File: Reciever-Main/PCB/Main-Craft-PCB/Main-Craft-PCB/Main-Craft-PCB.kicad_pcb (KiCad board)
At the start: 2 copper layers, 68.6 x 99.1 mm, 122 parts, among them J1 nRF24L01_Conn, J10 L298N, J2 IR_SENSOR_1, J3 IR_SENSOR_2, J4 IR_SENSOR_?, J5 IR_SENSOR_?, J6 ESC_1, J7 ESC_2, J8 ESC_3, J9 ESC_4, Q1 2N2219, Q10 2N2219, Q11 2N2219, Q12 2N2219, Q13 2N2219, Q14 2N2219, Q2 2N2219, Q3 2N2219, Q4 2N2219, Q5 2N2219, Q6 2N2219, Q7 2N2219, Q8 2N2219, Q9 2N2219, SW1 SW_Push, SW2 SW_Push, SW3 SW_SPDT, SW4 SW_SPDT, SW5 SW_SPDT, SW6 SW_SPDT, U1 NUCLEO144-F429ZI, U2 LM741, U3 LM741, U4 LM2940-3.0, U5 LM2940-5.0, U6 LM2940-12.0

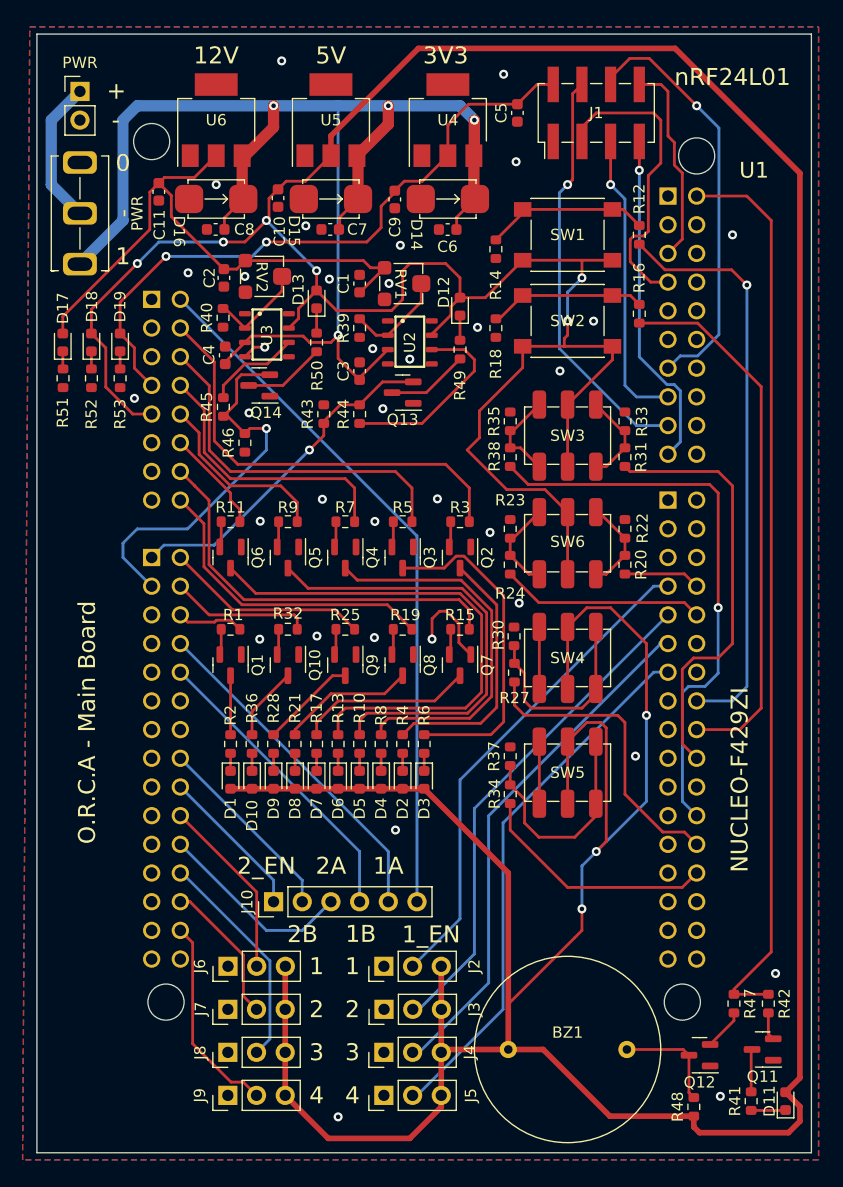
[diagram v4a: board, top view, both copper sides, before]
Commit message: Add Gerber files CPL files and update footprints for componetns
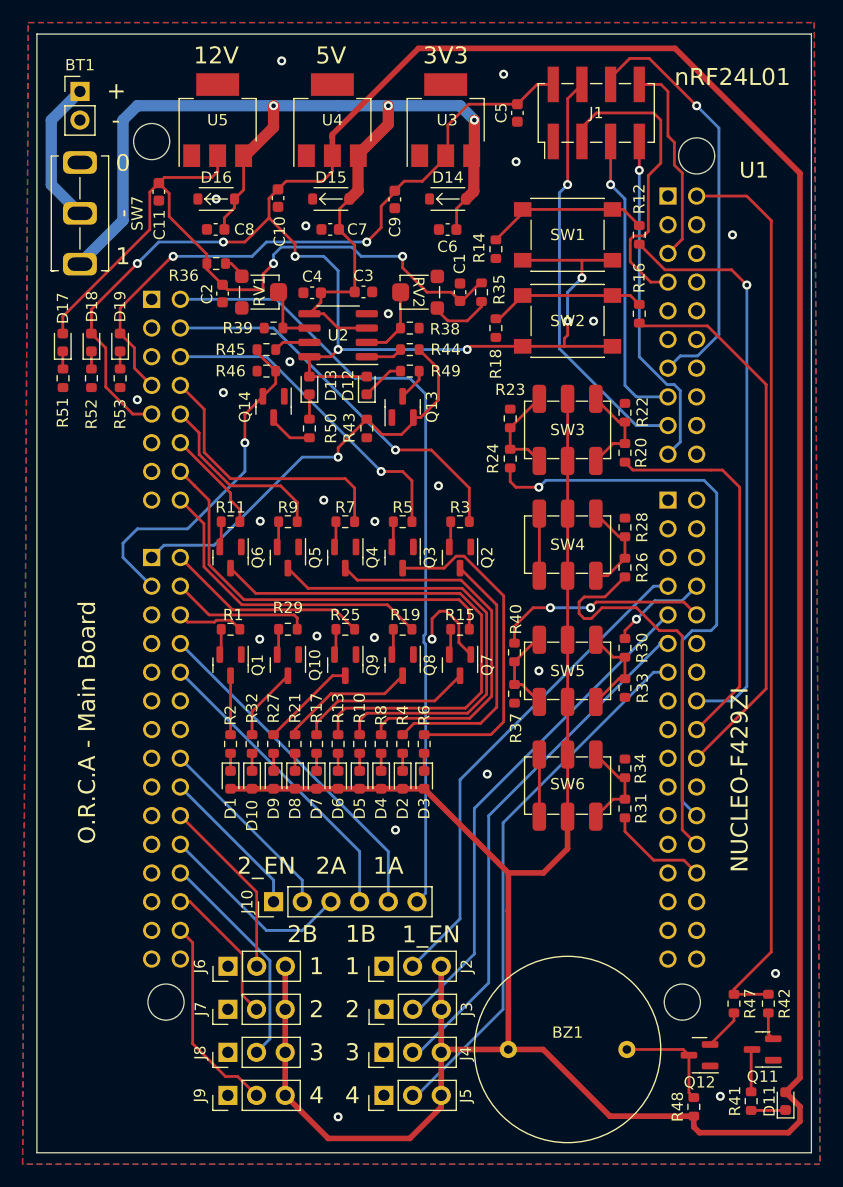
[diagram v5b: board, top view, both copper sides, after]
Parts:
- removed PWR: SW_SPDT, My_library:KNX-1-D1
- removed PWR: Battery, Connector_PinHeader_2.54mm:PinHeader_1x02_P2.54mm_Vertical
- removed U6: LM2940-12.0, Package_TO_SOT_SMD:SOT-223
- added BT1: Battery, Connector_PinHeader_2.54mm:PinHeader_1x02_P2.54mm_Vertical, F.Cu at (124.5, 55.9)
- added R26: 1K, Resistor_SMD:R_0603_1608Metric, F.Cu at (172.7, 98.0)
- added R29: 4K7, Resistor_SMD:R_0603_1608Metric, F.Cu at (142.9, 103.5)
- added SW7: SW_SPDT, My_library:KNX-1-D1, F.Cu at (124.5, 66.7)
- D1, D10, D17, D2, D3, D4, D5, D6, D7, D8, D9: value LED -> BLUE
- D11, D12, D19: value LED -> GREEN
- D13, D18: value LED -> YELLOW
- D14, D15, D16: footprint My_library:1N5817M -> My_library:SOD-123
- R10, R13, R17, R2, R21, R30, R4, R41, R49, R50, R6, R8: value 10K -> 1K
- R32: value 4K7 -> 1K
- R34: value 1K -> 10K
- R35, R36: value 10K -> 47K
- R38: value 1K -> 1M
- R40: value 1M -> 1K
- RV1: value 62K -> 15K; footprint My_library:35WR100KLFTR -> My_library:Variable_Resistor
- RV2: value 79K -> 32K; footprint My_library:35WR100KLFTR -> My_library:Variable_Resistor
- U2: value LM741 -> LM358DR2G; footprint My_library:741C -> Package_SO:SOP-8_3.76x4.96mm_P1.27mm
- U3: value LM741 -> LM2940-3.0; footprint My_library:741C -> Package_TO_SOT_SMD:SOT-223
- U4: value LM2940-3.0 -> LM2940-5.0
- U5: value LM2940-5.0 -> LM2940-12.0
- moved R36 42.7 mm to (136.5, 71.1), turned to 180 degrees
- moved R40 39.3 mm to (162.9, 105.6)
- moved R28 36.5 mm to (172.7, 94.5)
- moved R31 31.1 mm to (172.7, 119.4)
- moved U3 24.8 mm to (156.8, 58.4), turned to 90 degrees
- moved R33 23.6 mm to (172.7, 108.7), turned to -90 degrees
- moved R27 22.2 mm to (141.6, 113.7), turned to 90 degrees
- moved SW6 21.5 mm to (167.6, 117.3)
- moved R38 14.5 mm to (153.7, 76.8), turned to 180 degrees
- moved R35 11.7 mm to (160.0, 73.7)
- moved D12 10.8 mm to (149.9, 81.9)
- moved R32 10.6 mm to (139.7, 113.7), turned to 90 degrees
- moved R34 10.4 mm to (172.7, 115.8), turned to 90 degrees
- moved R22 10.3 mm to (172.7, 84.3)
- moved U4 10.2 mm to (146.8, 58.4)
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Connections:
- R20 pad 2: SW_7 -> SW_3
- R24 pad 2: SW_8 -> SW_4
- R27 pad 1: Net-(R27-Pad1) -> Net-(D9-Pad1)
- R27 pad 2: SW_5 -> Net-(Q9-Pad3)
- R28 pad 1: Net-(D9-Pad1) -> Net-(R26-Pad1)
- R28 pad 2: Net-(Q9-Pad3) -> Earth
- R30 pad 1: Net-(R27-Pad1) -> Net-(R30-Pad1)
- R30 pad 2: Earth -> SW_7
- R31 pad 2: SW_3 -> SW_6
- R32 pad 1: LED_10 -> Net-(D10-Pad1)
- R32 pad 2: Net-(Q10-Pad2) -> Net-(Q10-Pad3)
- R33 pad 1: Net-(R31-Pad1) -> Net-(R30-Pad1)
- R34 pad 1: Net-(R34-Pad1) -> Net-(R31-Pad1)
- R34 pad 2: SW_6 -> Earth
- R35 pad 2: Earth -> +12V
- R36 pad 1: Net-(D10-Pad1) -> Net-(R36-Pad1)
- R36 pad 2: Net-(Q10-Pad3) -> +12V
- R37 pad 1: Net-(R34-Pad1) -> Net-(R37-Pad1)
- R38 pad 1: Net-(R35-Pad1) -> Earth
- R38 pad 2: SW_4 -> Net-(R38-Pad2)
- R40 pad 1: Earth -> Net-(R37-Pad1)
- R40 pad 2: Net-(R40-Pad2) -> SW_8
- RV1 pad 1: +12V -> Net-(R35-Pad1)
- RV1 pad 2: Net-(R39-Pad2) -> Net-(R38-Pad2)
- RV2 pad 1: +12V -> Net-(R36-Pad1)
- RV2 pad 2: Net-(R40-Pad2) -> Net-(R39-Pad2)
- SW3 pad 1: Net-(R35-Pad1) -> Net-(R23-Pad1)
- SW3 pad 3: Net-(R31-Pad1) -> Net-(R20-Pad1)
- SW4 pad 3: Net-(R27-Pad1) -> Net-(R26-Pad1)
- SW5 pad 1: unconnected-(SW5-Pad1) -> Net-(R37-Pad1)
- SW5 pad 3: Net-(R34-Pad1) -> Net-(R30-Pad1)
- SW6 pad 1: Net-(R23-Pad1) -> unconnected-(SW6-Pad1)
- SW6 pad 3: Net-(R20-Pad1) -> Net-(R31-Pad1)
- U1 pad 112: SW_2 -> SW_3
- U1 pad 116: SW_3 -> SW_2
- U2 pad 1: unconnected-(U2-Pad1) -> Net-(R44-Pad1)
- U2 pad 2: Net-(R39-Pad2) -> Net-(R38-Pad2)
- U2 pad 5: unconnected-(U2-Pad5) -> +BATT
- U2 pad 6: Net-(R44-Pad1) -> Net-(R39-Pad2)
- U2 pad 7: +5V -> Net-(R45-Pad1)
- U2 pad 8: unconnected-(U2-Pad8) -> +5V
- U3 pad 1: unconnected-(U3-Pad1) -> Earth
- U3 pad 2: Net-(R40-Pad2) -> +3V3
- U3 pad 4: Earth -> (no net)
- U4 pad 2: +3V3 -> +5V
- U5 pad 2: +5V -> +12V
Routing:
- net +5V: track 479.7 -> 408.9 mm, vias 9 -> 7
- net +BATT: track 121.7 -> 99.5 mm, vias 4 -> 3
- net Net-(R34-Pad1): track 19.8 -> 0.00 mm
- net Net-(R27-Pad1): track 18.3 -> 0.00 mm
- net Net-(R44-Pad1): track 17.2 -> 3.25 mm
- net +12V: track 50.9 -> 64.6 mm, vias 0 -> 2
- net SW_6: track 21.5 -> 9.08 mm
- net SW_5: track 27.0 -> 35.7 mm
- net Net-(R40-Pad2): track 8.59 -> 0.00 mm
- net MOTOR_1_EN: track 62.0 -> 70.6 mm
- net Net-(R30-Pad1): track 0.00 -> 8.55 mm
- net Net-(R26-Pad1): track 0.00 -> 8.55 mm
- net Net-(R37-Pad1): track 0.00 -> 7.87 mm
- net BAT_15_PERCENT: track 30.3 -> 38.2 mm
- net Net-(R38-Pad2): track 0.00 -> 6.50 mm
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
